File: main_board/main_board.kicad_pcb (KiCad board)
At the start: 2 copper layers, 64.8 x 44.2 mm, 34 parts, among them J1 1-1734248-5, P1 USB_C_Plug_USB2.0, U2 ESP32-S3-WROOM-2, U3 MCP1700x-330xxTT

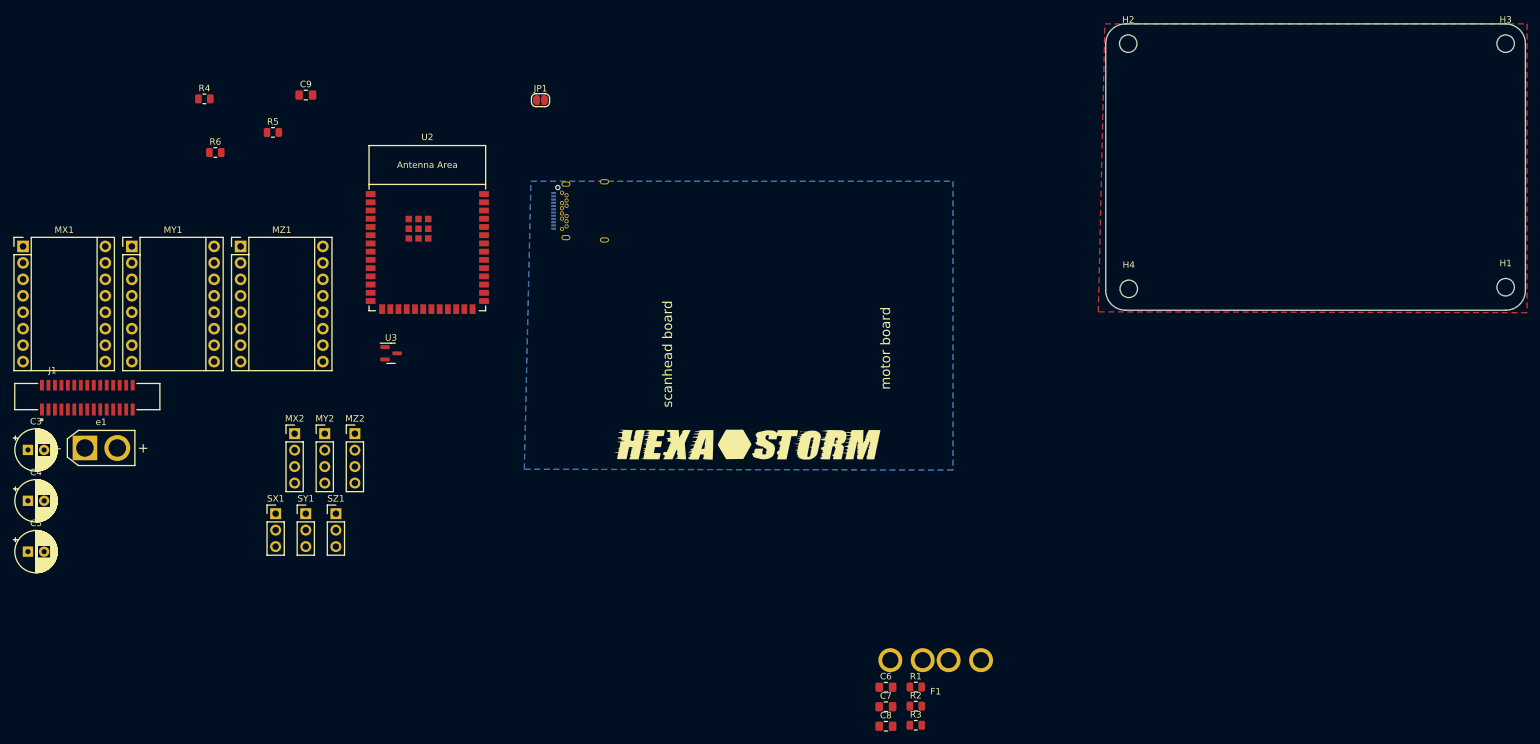
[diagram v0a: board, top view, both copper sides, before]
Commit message: started routing main board with esp32
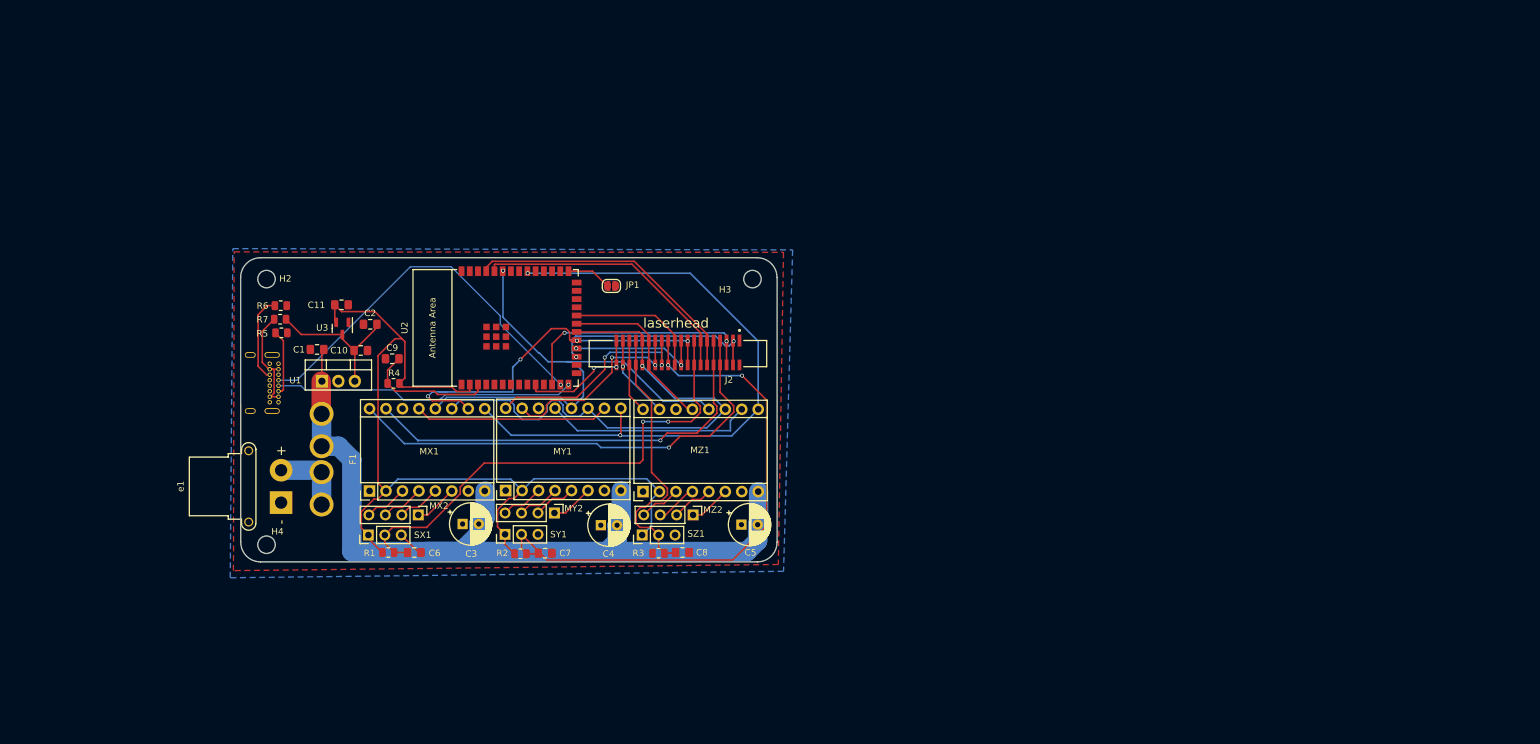
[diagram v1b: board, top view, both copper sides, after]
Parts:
- removed H1: MountingHole, MountingHole:MountingHole_2.7mm_M2.5
- removed J1: 1-1734248-5, footprints:TE_1-1734248-5
- added C1: 0.33mF, Capacitor_SMD:C_0805_2012Metric_Pad1.18x1.45mm_HandSolder, F.Cu at (162.8, 137.9)
- added C10: 1mF, Capacitor_SMD:C_0805_2012Metric_Pad1.18x1.45mm_HandSolder, F.Cu at (169.5, 138.0)
- added C11: 1mF, Capacitor_SMD:C_0805_2012Metric_Pad1.18x1.45mm_HandSolder, F.Cu at (166.6, 131.0)
- added C2: 0.1mF, Capacitor_SMD:C_0805_2012Metric_Pad1.18x1.45mm_HandSolder, F.Cu at (171.0, 134.0)
- added J2: 2-1734248-0, footprints:TE_2-1734248-0, F.Cu at (219.0, 138.5)
- added R7: 0K, Resistor_SMD:R_0805_2012Metric, F.Cu at (157.1, 133.2)
- added U1: LM7805_TO220, Package_TO_SOT_THT:TO-220-3_Vertical, F.Cu at (163.6, 142.8)
- G1: value hexastorm -> LOGO; moved to B.Cu
- P1: footprint Connector_USB:USB_C_Receptacle_Amphenol_12401548E4-2A -> footprints:USB_C_Receptacle_GCT_USB4085
- e1: footprint Connector_AMASS:AMASS_XT30U-F_1x02_P5.0mm_Vertical -> footprints:AMASS_XT30PW-F_1x02_P2.50mm_Horizontal
- moved H4 138.8 mm to (155.0, 168.0)
- moved H2 137.9 mm to (155.0, 127.0), turned to 180 degrees
- moved H3 122.1 mm to (230.0, 128.0)
- moved C5 110.2 mm to (228.3, 164.9)
- moved F1 99.7 mm to (163.5, 154.8), turned to 90 degrees
- moved C4 88.5 mm to (206.6, 165.0)
- moved R1 84.0 mm to (173.8, 169.2)
- moved C6 75.7 mm to (177.8, 169.2), turned to 180 degrees
- moved MZ1 72.7 mm to (213.1, 159.8), turned to 90 degrees
- moved MY1 68.9 mm to (191.9, 159.6), turned to 90 degrees
- moved C3 68.1 mm to (185.3, 164.8)
- moved MX1 65.5 mm to (170.9, 159.7), turned to 90 degrees
- moved R2 65.4 mm to (194.2, 169.4)
- moved C7 57.7 mm to (198.0, 169.3), turned to 180 degrees
- moved P1 55.9 mm to (156.8, 146.0), turned to 90 degrees
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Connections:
- P1 pad A4: +5V -> Net-(P1-VBUS-PadA4)
- P1 pad A9: +5V -> Net-(P1-VBUS-PadA4)
- P1 pad B4: +5V -> Net-(P1-VBUS-PadA4)
- P1 pad B9: +5V -> Net-(P1-VBUS-PadA4)
- U2 pad 10: SD_IO2 -> FREE
- U2 pad 11: SD_IO3 -> unconnected-(U2-GPIO18/U1RXD/ADC2_CH7/CLK_OUT3-Pad11)
- U2 pad 15: Z_PO -> unconnected-(U2-GPIO3/TOUCH3/ADC1_CH2-Pad15)
- U2 pad 33: Z_STEP -> unconnected-(U2-MTDO/GPIO40/CLK_OUT2-Pad33)
- U2 pad 34: Z_DIR -> unconnected-(U2-MTDI/GPIO41/CLK_OUT1-Pad34)
- U2 pad 38: Y_PO -> unconnected-(U2-GPIO2/TOUCH2/ADC1_CH1-Pad38)
- U2 pad 8: Y_STEP -> unconnected-(U2-GPIO15/U0RTS/ADC2_CH4/XTAL_32K_P-Pad8)
- U2 pad 9: Y_DIR -> unconnected-(U2-GPIO16/U0CTS/ADC2_CH5/XTAL_32K_N-Pad9)
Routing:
- net +3.3V: track 0.00 -> 140.1 mm
- net +12V: track 0.00 -> 132.4 mm
- net STEP_ENABLE: track 0.00 -> 100.4 mm, vias 0 -> 2
- net Y_PO: track 0.00 -> 87.5 mm, vias 0 -> 2
- net SPI_SCK: track 0.00 -> 81.5 mm, vias 0 -> 1
- net X_PO: track 0.00 -> 77.4 mm, vias 0 -> 2
- net SPI_SS3: track 0.00 -> 76.9 mm, vias 0 -> 1
- net X_DIR: track 0.00 -> 72.9 mm, vias 0 -> 1
- net X_STEP: track 0.00 -> 66.6 mm, vias 0 -> 1
- net SPI_SI: track 0.00 -> 60.1 mm, vias 0 -> 4
- net D-: track 0.00 -> 59.1 mm, vias 0 -> 1
- net D+: track 0.00 -> 46.7 mm, vias 0 -> 1
- net CFG_DONE: track 0.00 -> 44.5 mm
- net Z_PO: track 0.00 -> 42.7 mm
- net CFG_RST: track 0.00 -> 42.2 mm
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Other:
- board size 64.8 x 44.2 mm -> 82.8 x 46.9 mm
- board text added: "laserhead"
- board text removed: "motor board"
- board text removed: "scanhead board"

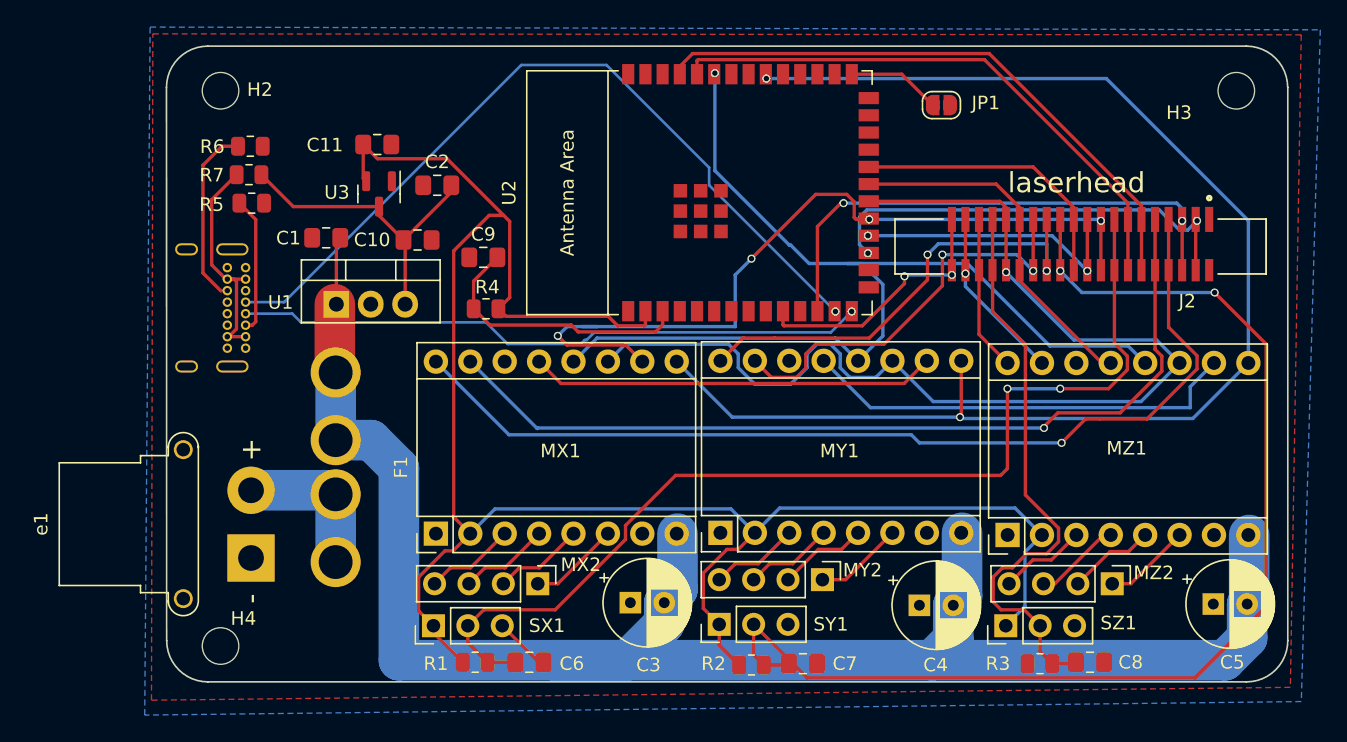
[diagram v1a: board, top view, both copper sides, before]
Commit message: finished routing main_board
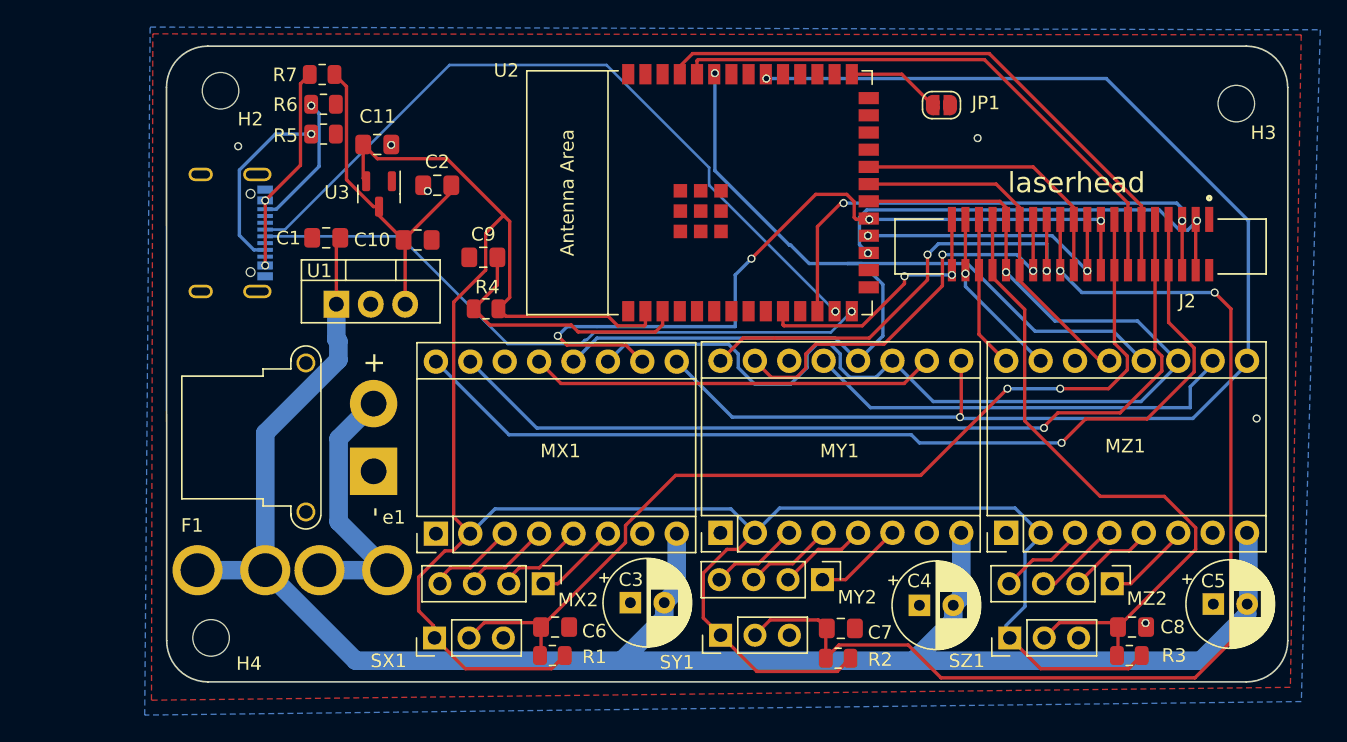
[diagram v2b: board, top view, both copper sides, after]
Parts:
- G1: value LOGO -> hexastorm
- P1: footprint footprints:USB_C_Receptacle_GCT_USB4085 -> Connector_USB:USB_C_Receptacle_GCT_USB4105-xx-A_16P_TopMnt_Horizontal
- moved e1 11.1 mm to (166.3, 155.1)
- moved R7 9.16 mm to (162.5, 125.8)
- moved P1 8.80 mm to (154.6, 137.5)
- moved F1 8.25 mm to (160.3, 162.4), turned to 180 degrees
- moved R5 7.36 mm to (162.6, 130.2)
- moved R3 6.63 mm to (222.1, 168.7), turned to 180 degrees
- moved R2 6.42 mm to (200.6, 168.9), turned to 180 degrees
- moved R6 6.23 mm to (162.6, 128.0)
- moved R1 5.72 mm to (179.5, 168.7), turned to 180 degrees
- moved C8 4.05 mm to (222.3, 166.6)
- moved C7 3.82 mm to (200.8, 166.7)
- moved C6 3.22 mm to (179.7, 166.6)
- moved SZ1 0.95 mm to (213.3, 167.4)
- moved H4 0.92 mm to (154.3, 167.4)
- moved SX1 0.90 mm to (170.8, 167.4)
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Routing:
- net +3.3V: track 140.1 -> 166.8 mm
- net Net-(e1-Pin_2): track 11.4 -> 19.9 mm
- net Z_PO: track 42.7 -> 49.6 mm
- net X_PO: track 77.4 -> 71.5 mm
- net Y_PO: track 87.5 -> 82.9 mm
- net GND: track 4.16 -> 0.00 mm, vias 0 -> 6
- net +12V: track 132.4 -> 136.5 mm
- net D-: track 59.1 -> 55.4 mm
- net Net-(P1-CC): track 10.1 -> 13.6 mm, vias 0 -> 1
- net Net-(P1-VCONN): track 13.5 -> 10.0 mm, vias 0 -> 1
- net +5V: track 23.2 -> 24.9 mm
- net Net-(P1-VBUS-PadA4): track 16.9 -> 15.5 mm, vias 0 -> 2
- net SPI_SI: track 60.1 -> 59.0 mm
- net D+: track 46.7 -> 47.6 mm

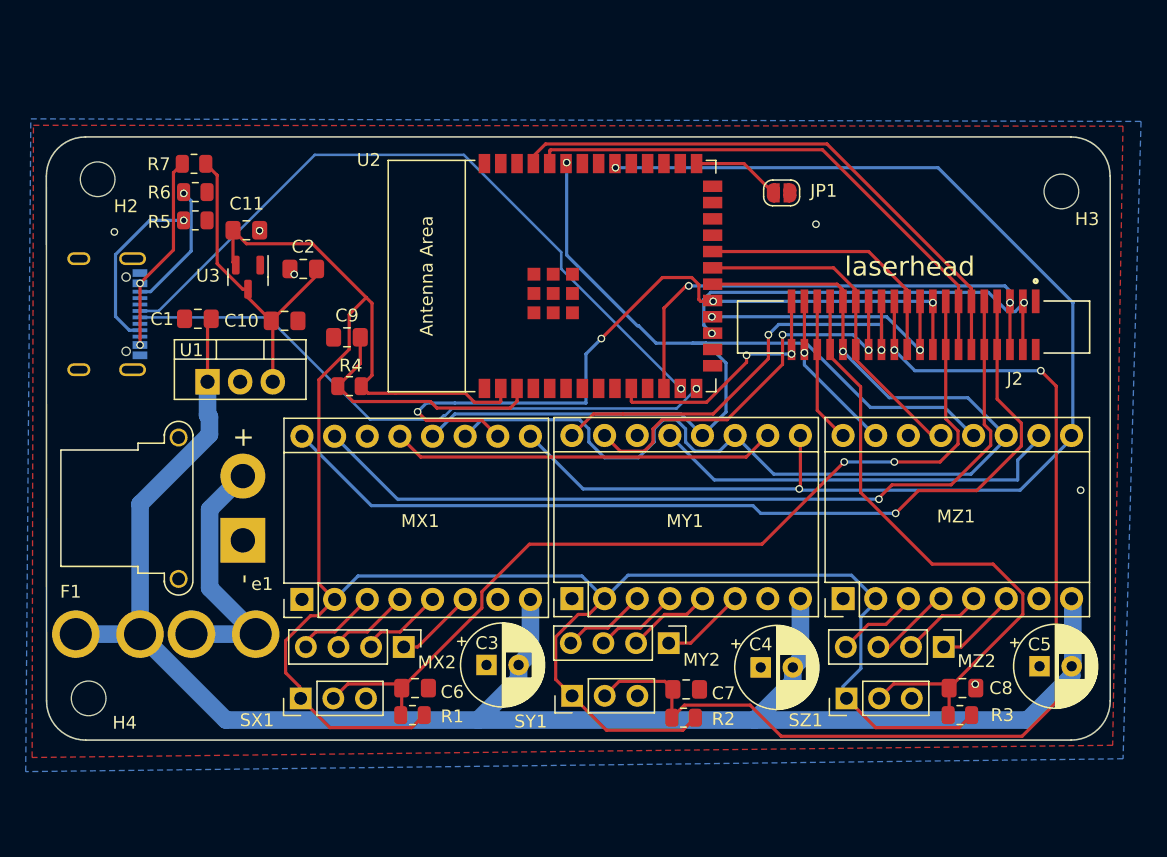
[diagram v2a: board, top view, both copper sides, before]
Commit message: started changing main board
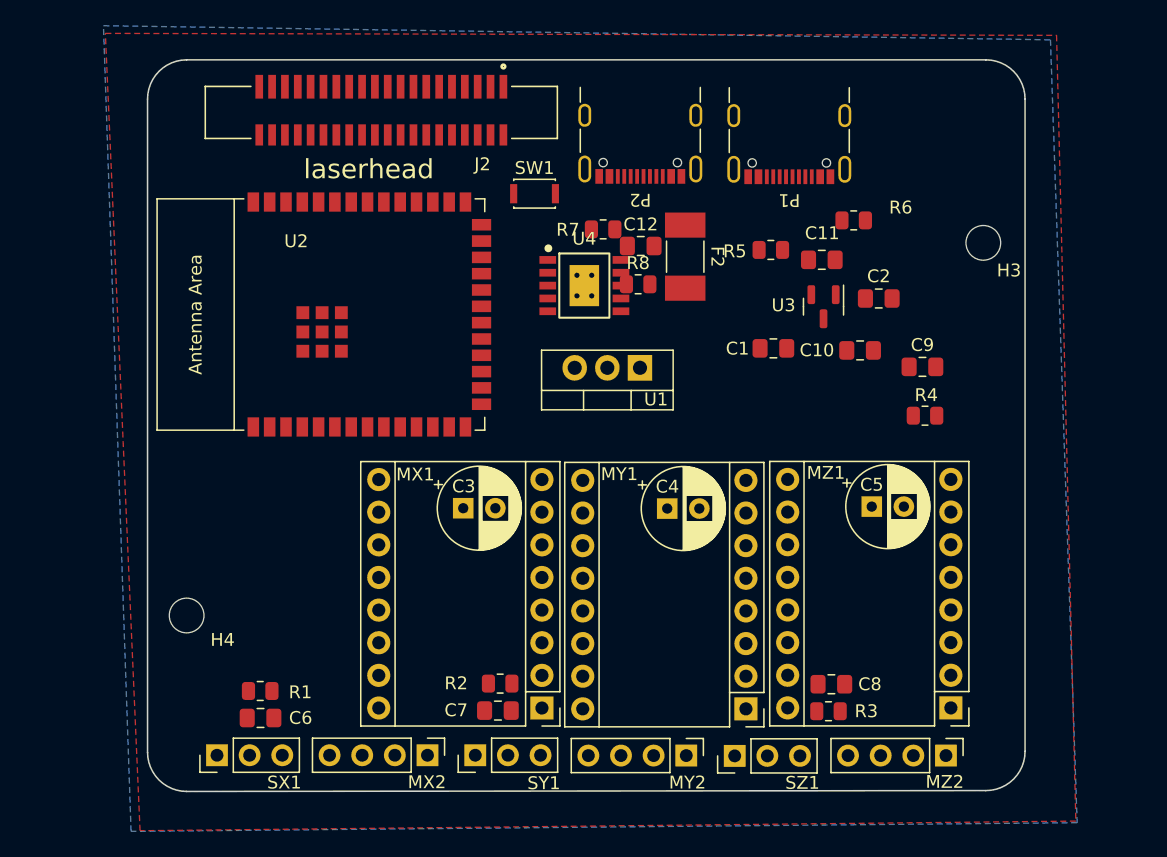
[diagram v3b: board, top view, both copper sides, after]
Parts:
- removed F1: 30A, footprints:MCCQ-121
- removed H2: MountingHole, MountingHole:MountingHole_2.7mm_M2.5
- removed JP1: Jumper_2_Open, Jumper:SolderJumper-2_P1.3mm_Open_RoundedPad1.0x1.5mm
- removed e1: Screw_Terminal_01x02, footprints:AMASS_XT30PW-F_1x02_P2.50mm_Horizontal
- added C12: 1uF, Capacitor_SMD:C_0805_2012Metric_Pad1.18x1.45mm_HandSolder, F.Cu at (197.3, 132.2)
- added F2: Fuse, Fuse:Fuse_Littelfuse-NANO2-451_453, F.Cu at (200.7, 133.0)
- added P2: USB_C_Plug_USB2.0, Connector_USB:USB_C_Receptacle_GCT_USB4105-xx-A_16P_TopMnt_Horizontal, F.Cu at (197.2, 123.1)
- added R8: 1K, Resistor_SMD:R_0805_2012Metric, F.Cu at (197.1, 135.2)
- added SW1: SW_Push_Open, footprints:SW_SPST_CK_KXT3, F.Cu at (189.0, 128.1)
- added U4: CH224K, footprints:ESSOP-10_CH224K, F.Cu at (192.9, 135.3)
- P1: moved to F.Cu
- R7: value 0K -> 10K
- moved P1 56.1 mm to (208.8, 123.1), turned to 180 degrees
- moved R6 51.3 mm to (213.8, 130.2)
- moved U3 44.8 mm to (211.5, 136.9)
- moved C1 44.8 mm to (207.6, 140.2)
- moved C10 44.8 mm to (214.3, 140.3)
- moved C11 44.8 mm to (211.4, 133.3)
- moved C2 44.8 mm to (215.8, 136.3)
- moved C9 44.8 mm to (219.2, 141.6)
- moved R4 44.8 mm to (219.4, 145.4)
- moved R5 44.8 mm to (207.4, 132.5)
- moved J2 44.7 mm to (177.6, 121.8)
- moved U1 33.7 mm to (197.2, 141.7), turned to 180 degrees
- moved R7 32.2 mm to (194.3, 130.9)
- moved MX1 20.5 mm to (189.6, 168.2), turned to 180 degrees
- moved U2 18.2 mm to (175.4, 137.5)
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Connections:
- P1 pad A4: Net-(P1-VBUS-PadA4) -> +5V
- P1 pad A8: (no net) -> unconnected-(P1-SBU1-PadA8)
- P1 pad A9: Net-(P1-VBUS-PadA4) -> +5V
- P1 pad B4: Net-(P1-VBUS-PadA4) -> +5V
- P1 pad B6: (no net) -> D+
- P1 pad B7: (no net) -> D-
- P1 pad B8: (no net) -> unconnected-(P1-SBU2-PadB8)
- P1 pad B9: Net-(P1-VBUS-PadA4) -> +5V
- R7 pad 1: Net-(P1-VBUS-PadA4) -> VBUS
- R7 pad 2: +5V -> Net-(U4-VBUS)
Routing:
- net +3.3V: track 166.8 -> 0.00 mm
- net +12V: track 136.5 -> 0.00 mm
- net STEP_ENABLE: track 100.3 -> 0.00 mm, vias 2 -> 0
- net Y_PO: track 82.9 -> 0.00 mm, vias 2 -> 0
- net SPI_SCK: track 81.5 -> 0.00 mm, vias 1 -> 0
- net SPI_SS3: track 76.9 -> 0.00 mm, vias 1 -> 0
- net X_DIR: track 72.7 -> 0.00 mm, vias 1 -> 0
- net X_PO: track 71.5 -> 0.00 mm, vias 2 -> 0
- net X_STEP: track 66.3 -> 0.00 mm, vias 1 -> 0
- net SPI_SI: track 59.0 -> 0.00 mm, vias 4 -> 0
- net D-: track 55.4 -> 0.00 mm, vias 1 -> 0
- net Z_PO: track 49.6 -> 0.00 mm
- net D+: track 47.6 -> 0.00 mm, vias 1 -> 0
- net CFG_DONE: track 44.5 -> 0.00 mm
- net CFG_RST: track 42.2 -> 0.00 mm
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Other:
- board size 82.8 x 46.9 mm -> 68.3 x 56.9 mm
